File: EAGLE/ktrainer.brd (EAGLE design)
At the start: 45.7 x 80 mm, 21 parts, among them IC1 DS3231/SO

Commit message: More PCB work
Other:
- board size 45.7 x 80 mm -> 45.7 x 77.5 mm
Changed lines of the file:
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@@
 <board>
 <plain>
-<wire x1="2.54" y1="0" x2="48.26" y2="0" width="0.4064" layer="20"/>
-<wire x1="48.26" y1="0" x2="48.26" y2="49.53" width="0.4064" layer="20"/>
-<wire x1="48.26" y1="49.53" x2="44.45" y2="49.53" width="0.4064" layer="20"/>
-<wire x1="44.45" y1="49.53" x2="44.45" y2="66.04" width="0.4064" layer="20"/>
-<wire x1="44.45" y1="66.04" x2="39.37" y2="66.04" width="0.4064" layer="20"/>
-<wire x1="39.37" y1="66.04" x2="39.37" y2="80.01" width="0.4064" layer="20"/>
-<wire x1="39.37" y1="80.01" x2="11.43" y2="80.01" width="0.4064" layer="20"/>
-<wire x1="11.43" y1="80.01" x2="11.43" y2="49.53" width="0.4064" layer="20"/>
-<wire x1="11.43" y1="49.53" x2="2.54" y2="49.53" width="0.4064" layer="20"/>
-<wire x1="2.54" y1="49.53" x2="2.54" y2="0" width="0.4064" layer="20"/>
+<wire x1="2.54" y1="1.27" x2="3.81" y2="0" width="0.4064" layer="20"/>
+<wire x1="3.81" y1="0" x2="46.99" y2="0" width="0.4064" layer="20"/>
+<wire x1="46.99" y1="0" x2="48.26" y2="1.27" width="0.4064" layer="20"/>
+<wire x1="48.26" y1="1.27" x2="48.26" y2="48.26" width="0.4064" layer="20"/>
+<wire x1="48.26" y1="48.26" x2="46.99" y2="49.53" width="0.4064" layer="20"/>
+<wire x1="46.99" y1="49.53" x2="44.45" y2="49.53" width="0.4064" layer="20"/>
+<wire x1="44.45" y1="49.53" x2="44.45" y2="64.77" width="0.4064" layer="20"/>
+<wire x1="44.45" y1="64.77" x2="43.18" y2="66.04" width="0.4064" layer="20"/>
+<wire x1="43.18" y1="66.04" x2="39.37" y2="66.04" width="0.4064" layer="20"/>
+<wire x1="39.37" y1="66.04" x2="39.37" y2="76.2" width="0.4064" layer="20"/>
+<wire x1="39.37" y1="76.2" x2="38.1" y2="77.47" width="0.4064" layer="20"/>
+<wire x1="38.1" y1="77.47" x2="12.7" y2="77.47" width="0.4064" layer="20"/>
+<wire x1="12.7" y1="77.47" x2="11.43" y2="76.2" width="0.4064" layer="20"/>
+<wire x1="11.43" y1="76.2" x2="11.43" y2="49.53" width="0.4064" layer="20"/>
+<wire x1="11.43" y1="49.53" x2="3.81" y2="49.53" width="0.4064" layer="20"/>
+<wire x1="3.81" y1="49.53" x2="2.54" y2="48.26" width="0.4064" layer="20"/>
+<wire x1="2.54" y1="48.26" x2="2.54" y2="1.27" width="0.4064" layer="20"/>
 <text x="19.05" y="57.15" size="0.889" layer="25" font="vector" ratio="12">kTrainer v1.0
 2017-04
@@
 <contactref element="U$3" pad="GND"/>
 <contactref element="U$3" pad="GND"/>
-<polygon width="0.4064" layer="1">
-<vertex x="3.81" y="35.56"/>
+<polygon width="0.4064" layer="1" isolate="0.3048">
+<vertex x="2.54" y="35.56"/>
 <vertex x="29.21" y="35.56"/>
 <vertex x="29.21" y="27.94"/>
-<vertex x="3.81" y="27.94"/>
-<vertex x="3.81" y="1.27"/>
-<vertex x="46.99" y="1.27"/>
-<vertex x="46.99" y="78.74"/>
-<vertex x="3.81" y="78.74"/>
+<vertex x="2.54" y="27.94"/>
+<vertex x="2.54" y="0"/>
+<vertex x="48.26" y="0"/>
+<vertex x="48.26" y="77.47"/>
+<vertex x="2.54" y="77.47"/>
 </polygon>
-<polygon width="0.4064" layer="16">
-<vertex x="3.81" y="78.74"/>
-<vertex x="3.81" y="35.56"/>
+<polygon width="0.4064" layer="16" isolate="0.3048">
+<vertex x="2.54" y="77.47"/>
+<vertex x="2.54" y="35.56"/>
 <vertex x="29.21" y="35.56"/>
 <vertex x="29.21" y="27.94"/>
-<vertex x="3.81" y="27.94"/>
-<vertex x="3.81" y="1.27"/>
-<vertex x="46.99" y="1.27"/>
-<vertex x="46.99" y="78.74"/>
+<vertex x="2.54" y="27.94"/>
+<vertex x="2.54" y="0"/>
+<vertex x="48.26" y="0"/>
+<vertex x="48.26" y="77.47"/>
 </polygon>
 <via x="19.05" y="43.18" extent="1-16" drill="0.6"/>

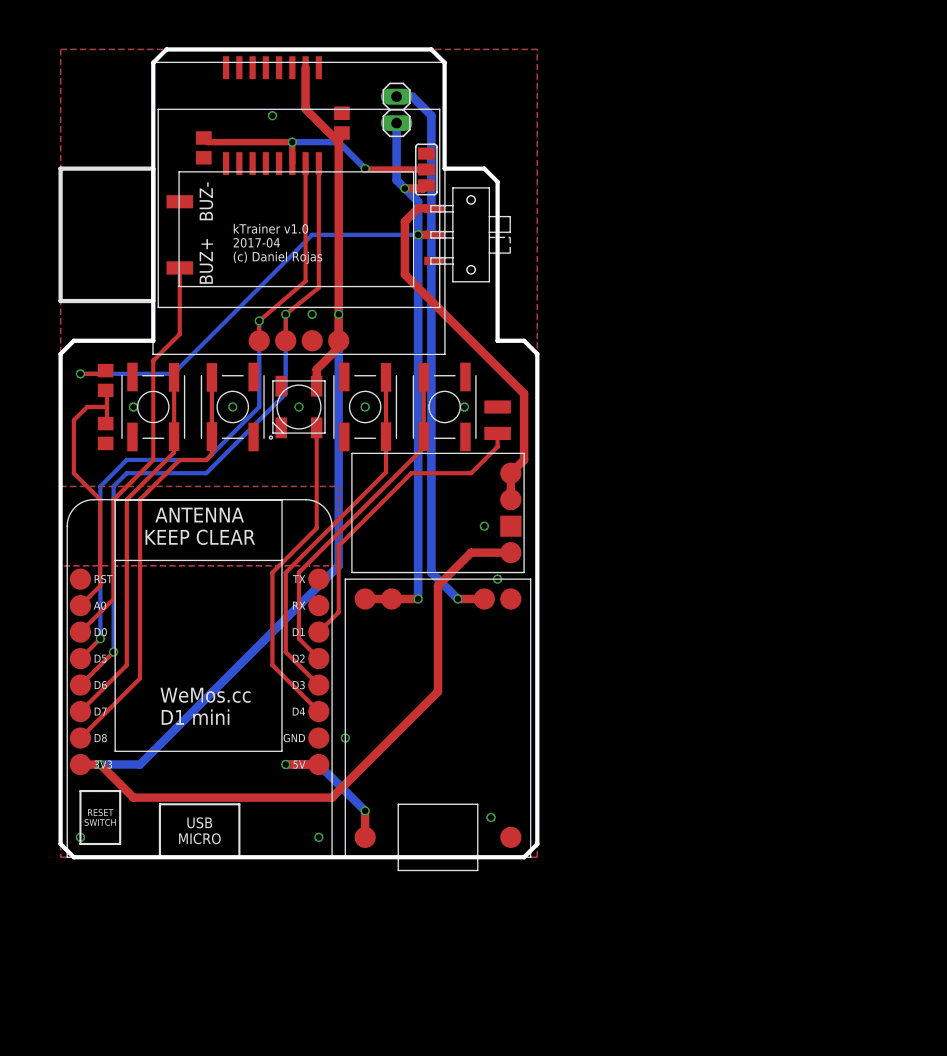
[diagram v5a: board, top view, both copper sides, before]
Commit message: Finish work on PCB, create gerber files and order on Seeed Studio
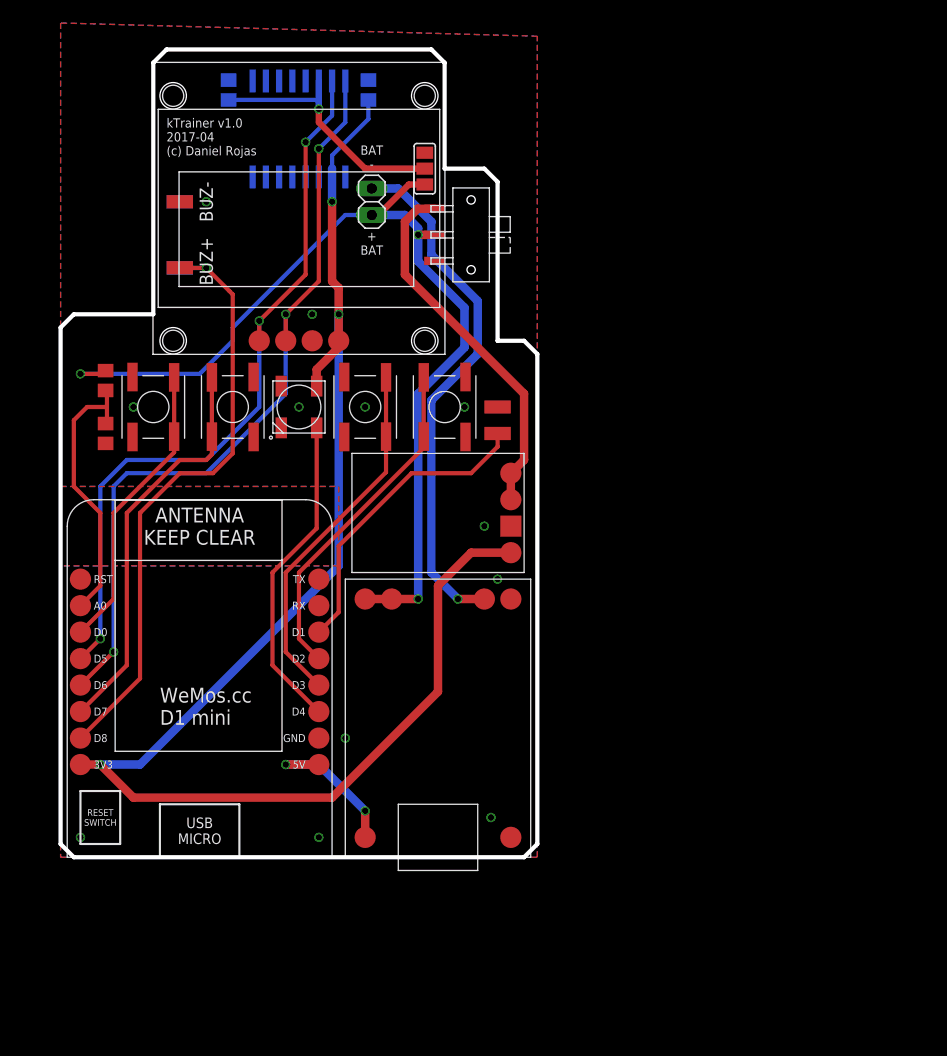
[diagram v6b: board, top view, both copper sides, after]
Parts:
- added BUZ+1, BUZ-1: (no value), wirepad:SMD1,27-2,54
- moved JP1 9.13 mm to (32.4, 62.9)
- moved C2 6.04 mm to (18.6, 73.6), flipped to the bottom, turned to 90 degrees
- moved C1 4.07 mm to (32.1, 73.6), flipped to the bottom
- moved IC1 2.84 mm to (25.4, 69.8), flipped to the bottom, turned to 0 degrees
- moved SJ1 0.17 mm to (37.5, 66.0)
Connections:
- net N$6 renamed B-
- net BUZ: now also BUZ+1.1, UC1.D8; no longer UC1.D0
- net GND: now also BUZ-1.1, IC1.10, IC1.11, IC1.12, IC1.5, IC1.6, IC1.7, IC1.8, IC1.9
- net PB1: now also UC1.D0; no longer UC1.D7
- net PB2: now also UC1.D7; no longer UC1.D8
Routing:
- net BUZ: track 38.9 -> 59.1 mm, vias 0 -> 1
- net SDA: track 63.0 -> 71.8 mm, vias 2 -> 3
- net SCL: track 66.7 -> 75.5 mm, vias 2 -> 3
- net PB1: track 35.8 -> 28.2 mm
- net B-: track 54.0 -> 50.5 mm
- net PB2: track 41.3 -> 38.8 mm
- net +3V3: track 147.2 -> 144.8 mm, vias 2 -> 3
- net VCC: track 95.8 -> 95.5 mm, vias 4 -> 3
- net VBAT: vias 2 -> 1
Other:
- outline, holes or cut-outs redrawn
- board text added: "+ BAT"
- board text added: "BAT -"

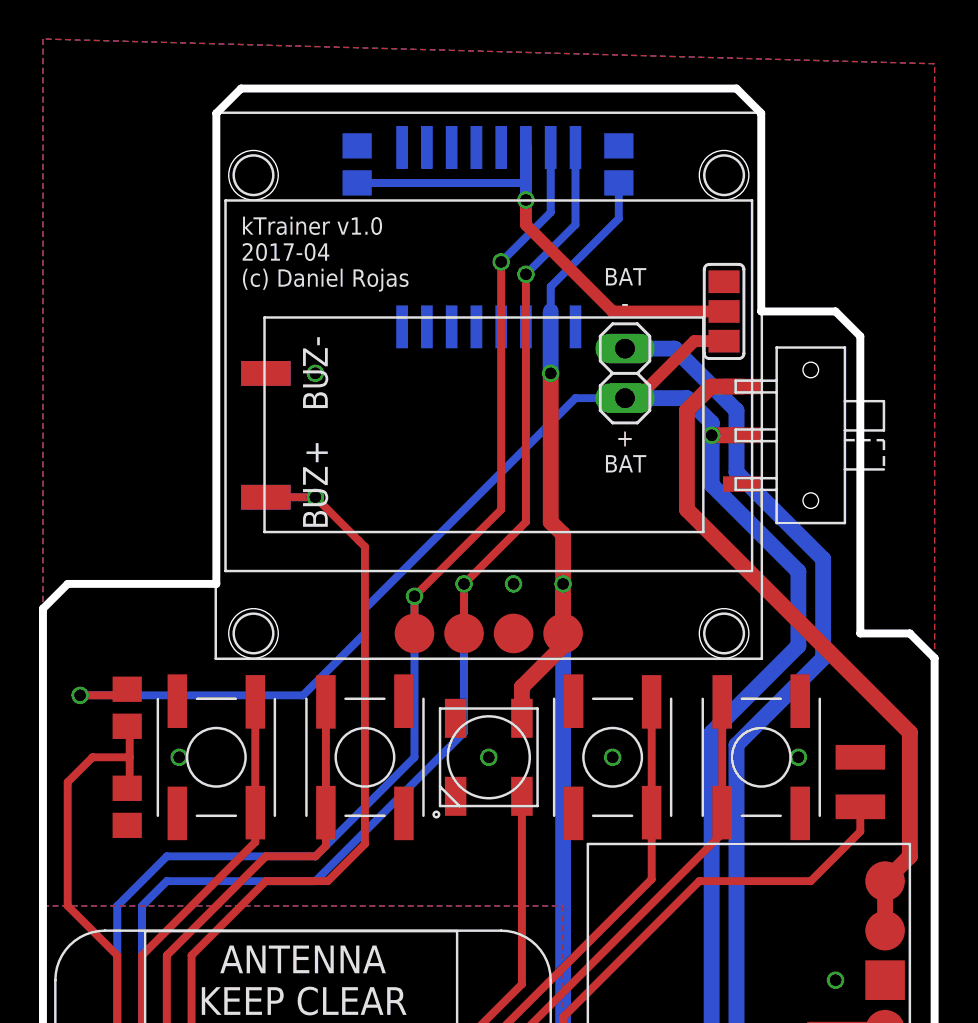
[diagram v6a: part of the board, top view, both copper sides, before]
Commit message: Annotate schematic: jumper wire from D1 to D0
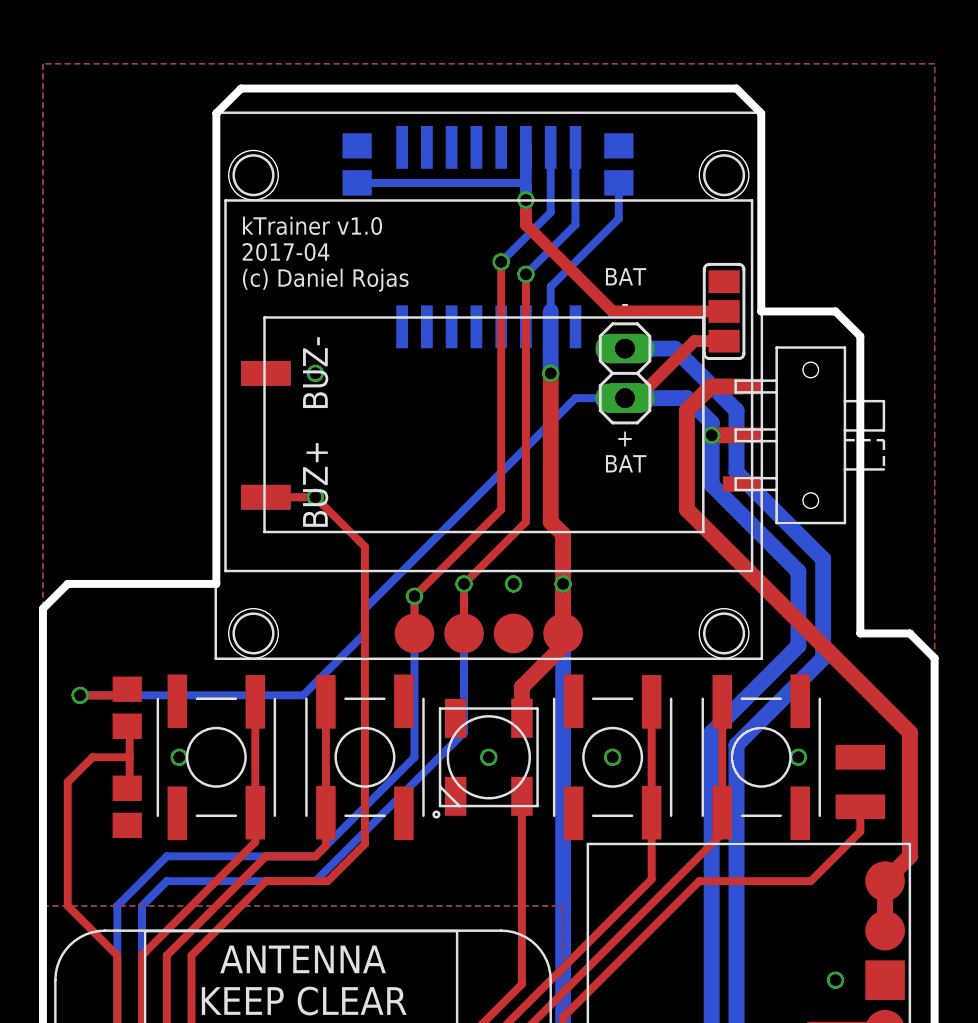
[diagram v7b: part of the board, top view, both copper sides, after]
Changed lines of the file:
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@@
 <layers>
 <layer number="1" name="Top" color="12" fill="1" visible="yes" active="yes"/>
-<layer number="16" name="Bottom" color="9" fill="1" visible="no" active="yes"/>
+<layer number="16" name="Bottom" color="9" fill="1" visible="yes" active="yes"/>
 <layer number="17" name="Pads" color="2" fill="1" visible="yes" active="yes"/>
 <layer number="18" name="Vias" color="2" fill="1" visible="yes" active="yes"/>
@@
 <vertex x="48.26" y="0"/>
 <vertex x="48.26" y="78.74"/>
-<vertex x="2.54" y="80.01"/>
+<vertex x="2.54" y="78.74"/>
 </polygon>
 <polygon width="0.4064" layer="16" isolate="0.3048">
-<vertex x="2.54" y="80.01"/>
+<vertex x="2.54" y="78.74"/>
 <vertex x="2.54" y="35.56"/>
 <vertex x="29.21" y="35.56"/>

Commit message: Set resistor values for ADC voltage divider
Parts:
- R1: value (none) -> 22k
- R2: value (none) -> 75k
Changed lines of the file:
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@@
 <?xml version="1.0" encoding="utf-8"?>
 <!DOCTYPE eagle SYSTEM "eagle.dtd">
-<eagle version="6.5.0">
+<eagle version="8.3.1">
 <drawing>
 <settings>
 <setting alwaysvectorfont="no"/>
+<setting keepoldvectorfont="yes"/>
 <setting verticaltext="up"/>
 </settings>
@@
 <pass name="Default">
 <param name="RoutingGrid" value="50mil"/>
+<param name="AutoGrid" value="1"/>
+<param name="Efforts" value="0"/>
+<param name="TopRouterVariant" value="1"/>
 <param name="tpViaShape" value="round"/>
 <param name="PrefDir.1" value="|"/>
@@
 <attribute name="VALUE" x="37.465" y="65.9399" size="0.02" layer="27" rot="R90"/>
 </element>
-<element name="R1" library="rcl" package="R0805" value="" x="6.858" y="45.72" smashed="yes" rot="R90">
+<element name="R1" library="rcl" package="R0805" value="22k" x="6.858" y="45.72" smashed="yes" rot="R90">
 <attribute name="VALUE" x="9.398" y="45.085" size="1.27" layer="27" rot="R90"/>
 </element>
-<element name="R2" library="rcl" package="R0805" value="" x="6.858" y="40.64" smashed="yes" rot="R90">
+<element name="R2" library="rcl" package="R0805" value="75k" x="6.858" y="40.64" smashed="yes" rot="R90">
 <attribute name="VALUE" x="9.398" y="40.005" size="1.27" layer="27" rot="R90"/>
 </element>
@@
 <element name="S1" library="formatc1702-switches" package="SWITCH-MSK12D04-SLIDER-SMD-PKG" value="" x="41.91" y="59.69" rot="R270"/>
 <element name="BUZ+" library="wirepad" package="SMD1,27-2,54" value="" x="13.97" y="56.515" smashed="yes" rot="R90">
+<attribute name="NAME" x="16.51" y="57.15" size="1.27" layer="25" font="vector" rot="R270" align="center"/>
 <attribute name="VALUE" x="13.97" y="56.515" size="0.0254" layer="27" rot="R90"/>
-<attribute name="NAME" x="16.51" y="57.15" size="1.27" layer="25" font="vector" rot="R270" align="center"/>
 </element>
 <element name="BUZ-" library="wirepad" package="SMD1,27-2,54" value="" x="13.97" y="62.865" smashed="yes" rot="R270">
+<attribute name="NAME" x="16.51" y="62.865" size="1.27" layer="25" font="vector" rot="R90" align="center"/>
 <attribute name="VALUE" x="13.97" y="62.865" size="0.0254" layer="27" rot="R270"/>
-<attribute name="NAME" x="16.51" y="62.865" size="1.27" layer="25" font="vector" rot="R90" align="center"/>
 </element>
 <element name="TP-AUX" library="wirepad" package="SMD1,27-2,54" value="" x="44.45" y="40.64" smashed="yes" rot="R90">
@@
 <contactref element="LED1" pad="VSS"/>
 <contactref element="IC1" pad="13"/>
-<contactref element="LED1" pad="VSS"/>
 <contactref element="UC1" pad="GND"/>
-<contactref element="IC1" pad="13"/>
 <contactref element="U$1" pad="OUT-"/>
 <contactref element="U$1" pad="IN-"/>
@@
 <contactref element="R2" pad="1"/>
 <contactref element="U$2" pad="GND"/>
-<contactref element="U$2" pad="GND"/>
-<contactref element="U$3" pad="GND"/>
 <contactref element="U$3" pad="GND"/>
 <polygon width="0.4064" layer="1" isolate="0.3048">
